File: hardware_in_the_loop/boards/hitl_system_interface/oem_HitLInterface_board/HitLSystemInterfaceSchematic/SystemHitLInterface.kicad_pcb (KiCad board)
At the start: 2 copper layers, 109.3 x 58.3 mm, 19 parts, among them U101 TPS560430YF

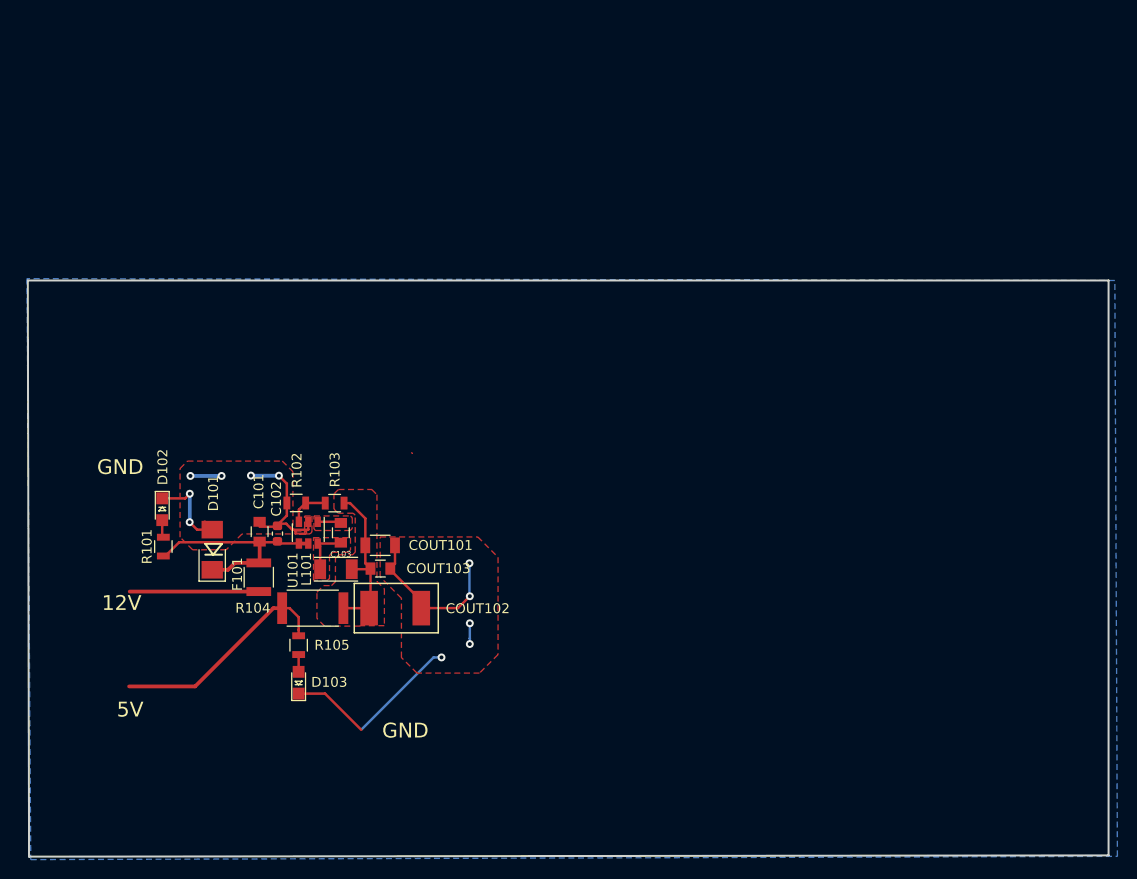
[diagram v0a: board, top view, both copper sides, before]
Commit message: PCB Layout Without USB_MicroB Footprint V1
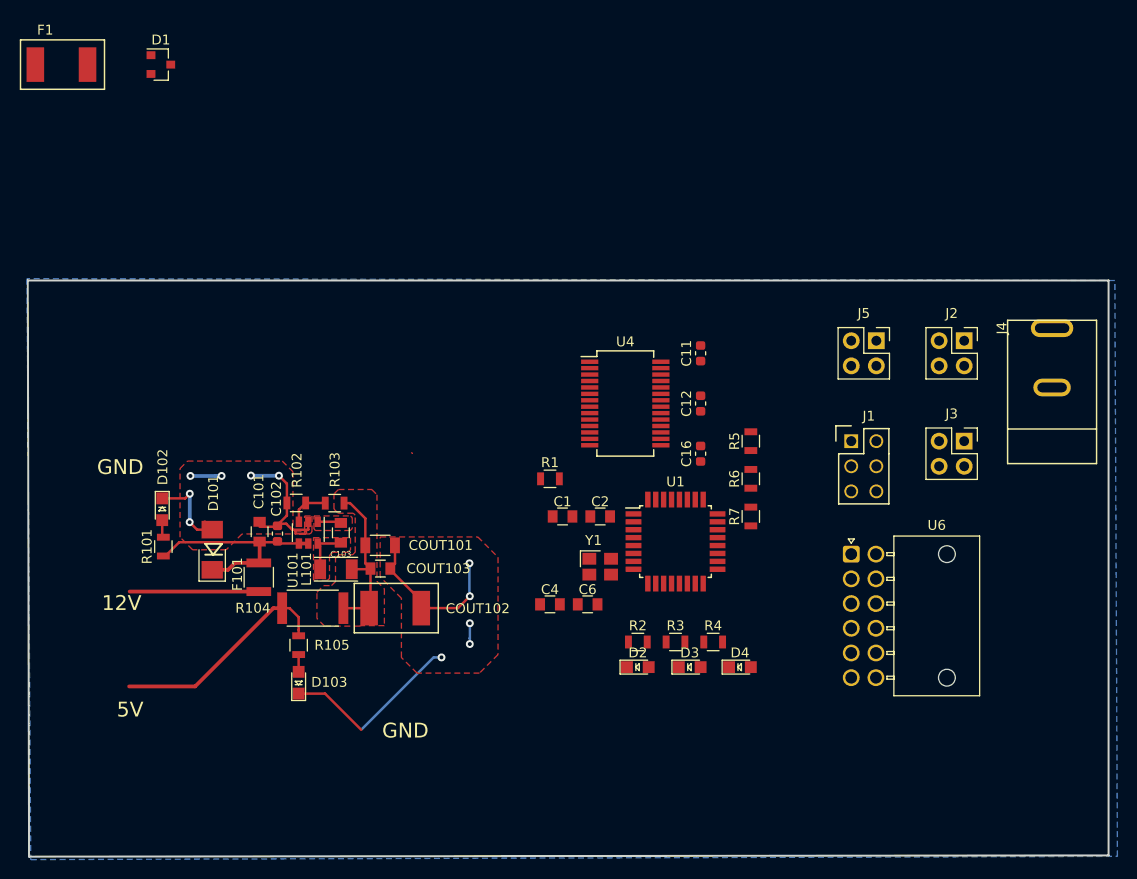
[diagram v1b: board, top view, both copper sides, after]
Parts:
- added C1: C_0.1uF, footprints:C_0805_OEM, F.Cu at (152.4, 100.3)
- added C11: C_4.7uF, footprints:C_0603_1608Metric, F.Cu at (166.4, 83.8)
- added C12: C_100nF, footprints:C_0603_1608Metric, F.Cu at (166.4, 88.9)
- added C16: C_100nF, footprints:C_0603_1608Metric, F.Cu at (166.4, 94.0)
- added C2: C_100pF, footprints:C_0805_OEM, F.Cu at (156.2, 100.3)
- added C4: C_30pF, footprints:C_0805_OEM, F.Cu at (151.1, 109.2)
- added C6: C_30pF, footprints:C_0805_OEM, F.Cu at (154.9, 109.2)
- added D1: BAS40-00, Package_TO_SOT_SMD:SOT-23, F.Cu at (111.8, 54.6)
- added D2: LED_0805, footprints:LED_0805_OEM, F.Cu at (160.0, 115.6)
- added D3: LED_0805, footprints:LED_0805_OEM, F.Cu at (165.3, 115.6)
- added D4: LED_0805, footprints:LED_0805_OEM, F.Cu at (170.3, 115.6)
- added F1: 200mA_Fuse, footprints:Fuse_1812, F.Cu at (99.1, 54.6)
- added J1: CONN_02X03, footprints:Pin_Header_Straight_2x03, F.Cu at (181.6, 92.7)
- added J2: Conn_01x04_Female, formula:PinSocket_2x02_P2.54mm_Vertical, F.Cu at (193.0, 82.5)
- added J3: Conn_01x04_Female, formula:PinSocket_2x02_P2.54mm_Vertical, F.Cu at (193.0, 92.7)
- added J4: Barrel_Jack, formula:barrel_jack_PJ-037A, F.Cu at (201.9, 81.3)
- added J5: Conn_01x04_Female, formula:PinSocket_2x02_P2.54mm_Vertical, F.Cu at (184.2, 82.5)
- added R1: R_100, footprints:R_0805_OEM, F.Cu at (151.1, 96.5)
- added R2: R_200, footprints:R_0805_OEM, F.Cu at (160.0, 113.0)
- added R3: R_200, footprints:R_0805_OEM, F.Cu at (163.8, 113.0)
- added R4: R_200, footprints:R_0805_OEM, F.Cu at (167.6, 113.0)
- added R5: R_10K, footprints:R_0805_OEM, F.Cu at (171.4, 92.7)
- added R6: R_10K, footprints:R_0805_OEM, F.Cu at (171.4, 96.5)
- added R7: R_10K, footprints:R_0805_OEM, F.Cu at (171.4, 100.3)
- added U1: ATmega328P-AU, Package_QFP:TQFP-32_7x7mm_P0.8mm, F.Cu at (163.8, 102.9)
- added U4: FT232RL, Package_SO:SSOP-28_5.3x10.2mm_P0.65mm, F.Cu at (158.8, 88.9)
- added U6: NanoFit_RA_TH_12, footprints:NanoFit_RA_12, F.Cu at (181.6, 104.1)
- added Y1: Crystal_SMD, footprints:Crystal_SMD_FA238, F.Cu at (156.2, 105.4)

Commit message: PCB Layout V2
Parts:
- added U3: USB_MicroB, Connector_USB:USB_Micro-B_Molex-105133-0031, F.Cu at (170.2, 82.5)
- moved J2 100.0 mm to (104.1, 128.3)
- moved J4 90.9 mm to (119.4, 119.4)
- moved J5 82.6 mm to (101.6, 80.0), turned to 90 degrees
- moved F1 82.1 mm to (175.3, 85.1)
- moved D1 67.9 mm to (175.3, 78.7), turned to 180 degrees
- moved J3 39.1 mm to (201.9, 130.8), turned to 180 degrees
- moved J1 27.9 mm to (162.6, 113.0)
- moved D4 21.5 mm to (149.9, 122.1), turned to 270 degrees
- moved R4 16.5 mm to (152.4, 119.4), turned to 270 degrees
- moved D3 15.5 mm to (149.9, 117.0), turned to 270 degrees
- moved U6 13.1 mm to (175.3, 92.7)
- moved R7 12.7 mm to (161.3, 92.7)
- moved C16 11.7 mm to (163.8, 82.5)
- moved R3 11.7 mm to (152.4, 115.6), turned to 270 degrees
- moved D2 10.9 mm to (149.9, 111.8), turned to 270 degrees
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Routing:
- net /12V: track 13.1 -> 33.1 mm
- net Net-(D3-Pad2): track 0.00 -> 4.54 mm
- net Net-(D2-Pad2): track 0.00 -> 3.39 mm
- net Net-(D4-Pad2): track 0.00 -> 2.26 mm

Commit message: PCB Layout V2
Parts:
- moved U6 20.7 mm to (189.2, 108.0), turned to 180 degrees
- moved J4 12.7 mm to (119.4, 132.1), turned to 270 degrees
- moved F1 4.58 mm to (179.1, 87.6)
- moved D1 4.02 mm to (179.1, 80.0)
- moved U3 1.27 mm to (171.4, 82.5), turned to 180 degrees
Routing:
- net VCC: track 22.7 -> 178.8 mm, vias 0 -> 14
- net /D5: track 0.00 -> 109.1 mm, vias 0 -> 2
- net /SDA: track 0.00 -> 80.1 mm, vias 0 -> 2
- net /SCL: track 0.00 -> 72.4 mm, vias 0 -> 2
- net /SCK: track 0.00 -> 62.4 mm, vias 0 -> 2
- net /MISO: track 0.00 -> 58.9 mm, vias 0 -> 2
- net /MOSI: track 0.00 -> 51.0 mm
- net /D2: track 0.00 -> 48.3 mm
- net /RESET: track 0.00 -> 40.4 mm, vias 0 -> 2
- net /D6: track 0.00 -> 39.7 mm, vias 0 -> 2
- net GND: track 65.5 -> 104.9 mm, vias 11 -> 34
- net /D1: track 0.00 -> 39.3 mm
- net /D4: track 0.00 -> 34.6 mm, vias 0 -> 2
- net /AI3: track 0.00 -> 33.7 mm, vias 0 -> 2
- net /D3: track 0.00 -> 31.5 mm, vias 0 -> 2
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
